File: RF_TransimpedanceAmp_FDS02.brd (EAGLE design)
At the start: 69.8 x 38.1 mm, 38 parts, among them IC1 PMA-5452, IC2 PMA-5452, IC3 PMA-5452, IC4 ADM7150ARDZ-3.0, IC5 ADM7150ARDZ-5.0, X1 SMAJ502

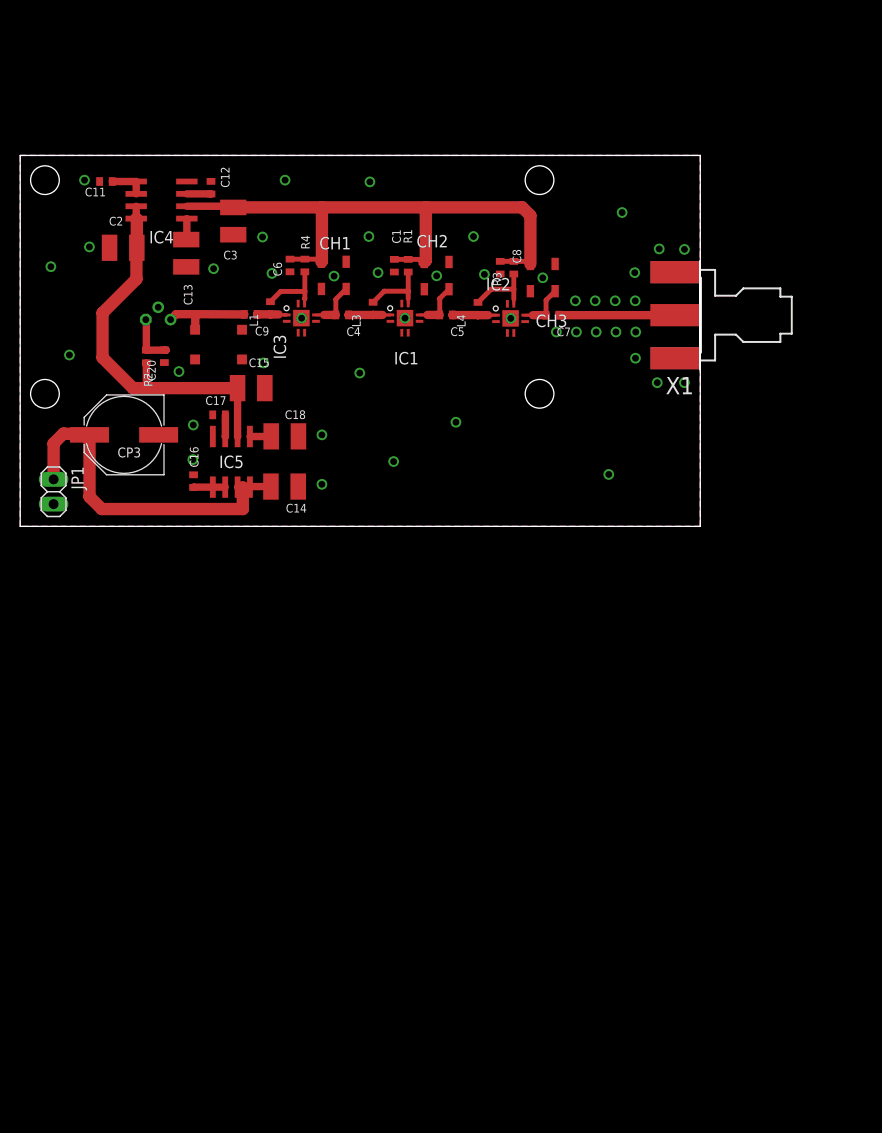
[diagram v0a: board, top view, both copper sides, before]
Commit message: Ripped up traces in preparation for adding additional SMA and switch for beatnote
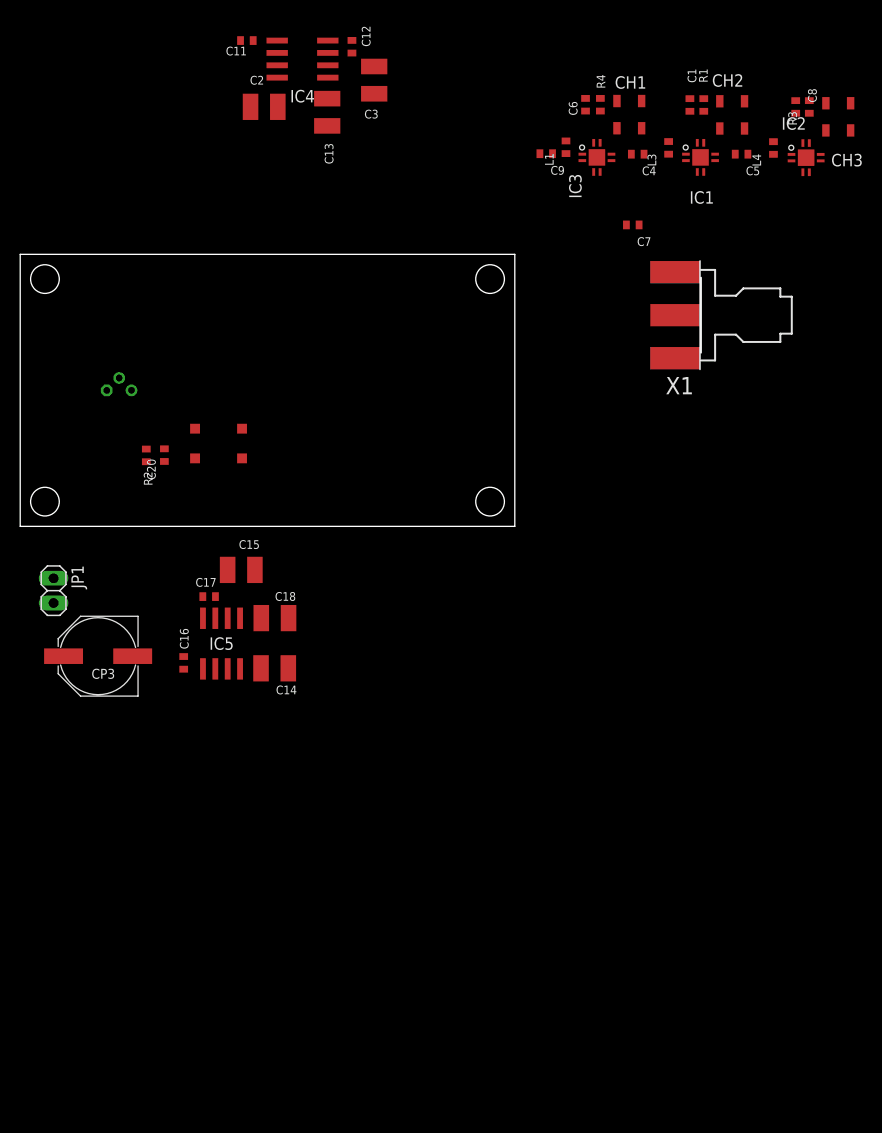
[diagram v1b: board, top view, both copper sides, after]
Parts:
- moved C5 34.6 mm to (74.1, 38.2)
- moved C6 34.6 mm to (58.1, 43.3)
- moved C9 34.6 mm to (54.0, 38.3)
- moved IC1 34.6 mm to (69.9, 37.0)
- moved IC3 34.6 mm to (59.2, 37.0)
- moved L1 34.6 mm to (56.1, 38.9)
- moved R3 34.6 mm to (81.1, 43.1)
- moved R4 34.6 mm to (59.6, 43.3)
- moved C1 34.6 mm to (68.8, 43.3)
- moved C4 34.6 mm to (63.4, 38.2)
- moved C8 34.6 mm to (79.7, 43.1)
- moved CH1 34.6 mm to (62.6, 42.3)
- moved CH2 34.6 mm to (73.1, 42.3)
- moved CH3 34.6 mm to (84.0, 42.1)
- moved IC2 34.6 mm to (80.7, 36.9)
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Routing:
- net +3V: track 61.7 -> 0.00 mm
- net +5V: track 41.2 -> 0.00 mm
- net +15V: track 36.2 -> 0.00 mm
- net N$4: track 11.9 -> 0.00 mm
- net N$7: track 9.42 -> 0.00 mm
- net N$3: track 7.32 -> 0.00 mm
- net N$10: track 7.30 -> 0.00 mm
- net N$9: track 7.24 -> 0.00 mm
- net N$5: track 5.37 -> 0.00 mm
- net N$6: track 5.15 -> 0.00 mm
- net N$2: track 5.10 -> 0.00 mm
- net N$8: track 4.99 -> 0.00 mm
- net RFPD2: track 4.49 -> 0.00 mm
- net RFPD1: track 4.30 -> 0.00 mm
- net N$1: track 3.73 -> 0.00 mm
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- removed copper zone on layer 1, net GND
- removed copper zone on layer 16, net GND
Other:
- board size 69.8 x 38.1 mm -> 50.8 x 27.9 mm

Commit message: Added SMA photodiode input; output monitor
Switch between FDS02 or other photodiode by soldering 0ohm jumper.
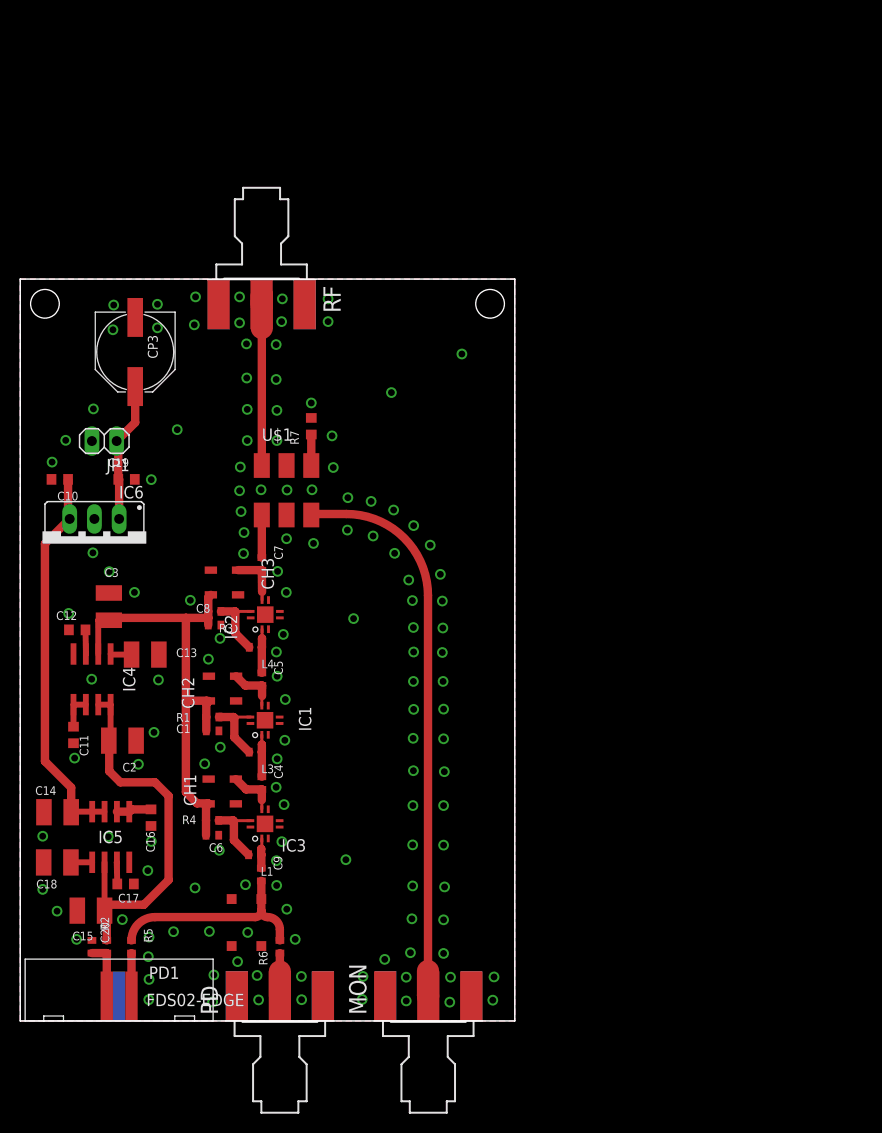
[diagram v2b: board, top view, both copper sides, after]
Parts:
- removed X1: SMAJ502, connector-jqi:SMA-EDGE
- added C10: 100nF, rlc-jqi:0603
- added C19: 1uF, rlc-jqi:0603
- added IC6: (no value), regulator-jqi:TO220
- added MON, PD: SMAJ502-bulkhead, connector-jqi:SMA-EDGE
- added R5, R6: 0R, rlc-jqi:0402
- added R7: 50R, rlc-jqi:0603
- added RF: SMAJ502, connector-jqi:SMA-EDGE
- added U$1: ADC-10-4, RF_TransimpedanceAmp:BH292
- C11, C12, C16, C17: device rlc-jqi:0402 -> rlc-jqi:0603
- CP3: value (none) -> 220uF
- PD1: value FDS02 -> FDS02-EDGE; device semiconductor-jqi:FDS02 -> RF_TransimpedanceAmp:FDS02-SIDEMOUNT
- moved C6 84.3 mm to (19.7, -31.7), turned to 0 degrees
- moved R4 83.6 mm to (19.7, -30.2), turned to 180 degrees
- moved CH1 81.1 mm to (20.8, -27.2), turned to 270 degrees
- moved C1 80.8 mm to (19.8, -21.0), turned to 0 degrees
- moved R1 80.6 mm to (19.8, -19.6), turned to 180 degrees
- moved R3 80.1 mm to (20.0, -8.74), turned to 180 degrees
- moved C8 80.0 mm to (20.0, -10.1), turned to 0 degrees
- moved C9 79.6 mm to (24.8, -35.8), turned to 270 degrees
- moved L1 79.4 mm to (24.1, -33.7), turned to 180 degrees
- moved CH3 79.1 mm to (21.0, -5.77), turned to 270 degrees
- moved CH2 78.8 mm to (20.8, -16.7), turned to 270 degrees
- moved C4 75.3 mm to (24.8, -26.4), turned to 270 degrees
- moved IC3 75.2 mm to (26.1, -30.6), turned to 90 degrees
- moved L3 75.2 mm to (24.2, -23.2), turned to 180 degrees
- moved L4 73.9 mm to (24.2, -12.4), turned to 180 degrees
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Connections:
- new net N$11: C7.1, U$1.P1
- new net N$12: MON.1, U$1.P3
- new net N$16: PD1.P$3, R5.2
- new net N$17: PD.1, R6.1
- new net N$20: R7.1, U$1.P4
- new net V+: C10.1, C14.1, IC5.7, IC5.8, IC6.3
- net +15V: now also C19.1, IC6.1; no longer C14.1, IC5.7, IC5.8
- net GND: now also C10.2, C19.2, IC6.2, MON.G@1, MON.G@2, MON.G@3, MON.G@4, PD.G@1, PD.G@2, PD.G@3, PD.G@4, R7.2, RF.G@1, RF.G@2, RF.G@3, RF.G@4, U$1.P2; no longer X1.G@1, X1.G@2, X1.G@3, X1.G@4
- net N$4: now also RF.1, U$1.P6; no longer C7.1, X1.1
- net N$7: now also R5.1, R6.2; no longer PD1.P$3
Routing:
- net N$12: track 0.00 -> 56.6 mm
- net +3V: track 0.00 -> 47.7 mm
- net V+: track 0.00 -> 40.0 mm
- net +5V: track 0.00 -> 39.8 mm
- net N$7: track 0.00 -> 21.5 mm
- net N$4: track 0.00 -> 18.6 mm
- net +15V: track 0.00 -> 14.6 mm
- net N$3: track 0.00 -> 7.46 mm
- net N$9: track 0.00 -> 7.39 mm
- net N$10: track 0.00 -> 7.33 mm
- net N$5: track 0.00 -> 5.95 mm
- net N$8: track 0.00 -> 5.50 mm
- net N$6: track 0.00 -> 5.15 mm
- net N$2: track 0.00 -> 5.12 mm
- net RFPD2: track 0.00 -> 4.50 mm
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- added copper zone on layer 1, net GND
- added copper zone on layer 16, net GND
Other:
- board size 50.8 x 27.9 mm -> 50.8 x 76.2 mm
